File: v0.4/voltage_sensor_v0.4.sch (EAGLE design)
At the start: 56 parts, among them IC1 AP2112K-3.3TRG1, J1 1017505, J2 20020316-H021B01LF, J9 RJ11-6, M1 MOV-14D431KTR, M2 MOV-14D431KTR, M3 MOV-14D431KTR, T1 ZMPT101B, T2 ZMPT101B, T3 ZMPT101B

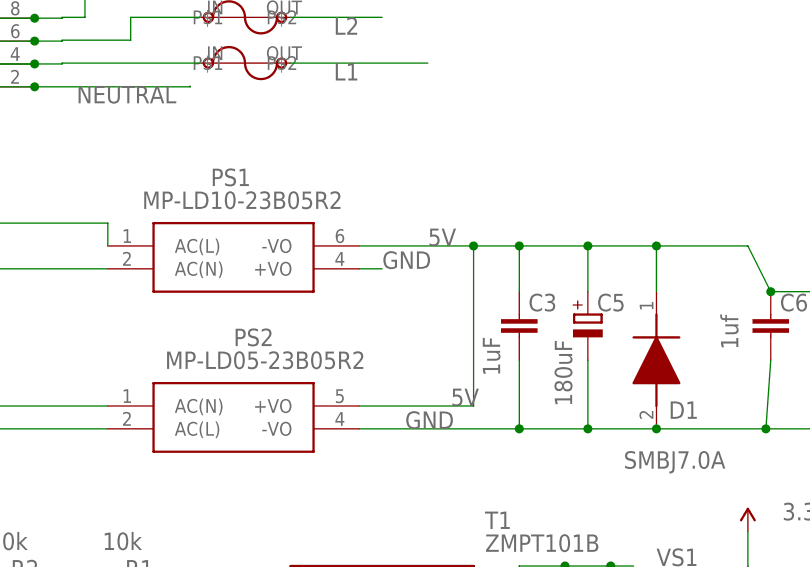
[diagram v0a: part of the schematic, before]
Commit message: fix PSU 10W footprint
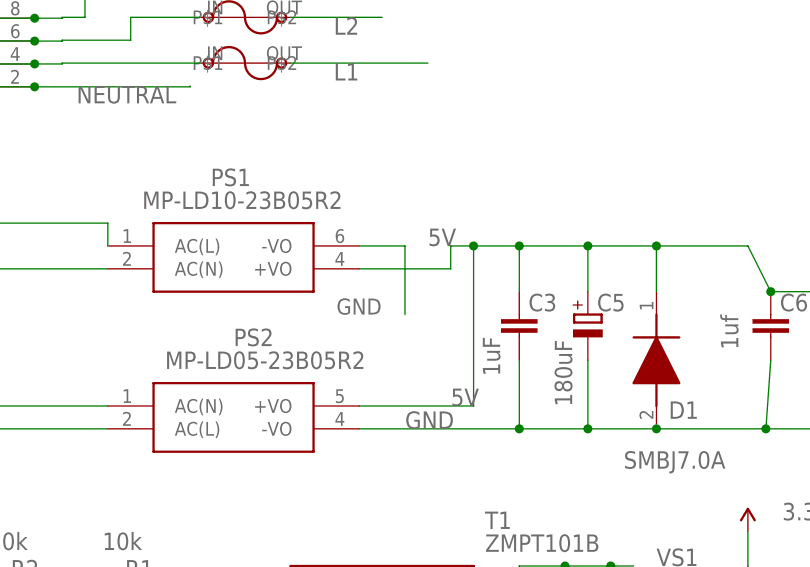
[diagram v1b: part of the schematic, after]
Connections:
- net 5V: now also PS1.+VO; no longer PS1.-VO
- net GND: now also PS1.-VO; no longer PS1.+VO
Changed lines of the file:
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@@
 <grid distance="0.1" unitdist="inch" unit="inch" style="lines" multiple="1" display="no" altdistance="0.01" altunitdist="inch" altunit="inch"/>
 <layers>
-<layer number="1" name="Top" color="4" fill="1" visible="yes" active="no"/>
-<layer number="16" name="Bottom" color="1" fill="1" visible="yes" active="no"/>
-<layer number="17" name="Pads" color="2" fill="1" visible="yes" active="no"/>
-<layer number="18" name="Vias" color="2" fill="1" visible="yes" active="no"/>
-<layer number="19" name="Unrouted" color="6" fill="1" visible="yes" active="no"/>
-<layer number="20" name="Dimension" color="24" fill="1" visible="yes" active="no"/>
-<layer number="21" name="tPlace" color="7" fill="1" visible="yes" active="no"/>
-<layer number="22" name="bPlace" color="7" fill="1" visible="yes" active="no"/>
-<layer number="23" name="tOrigins" color="15" fill="1" visible="yes" active="no"/>
-<layer number="24" name="bOrigins" color="15" fill="1" visible="yes" active="no"/>
-<layer number="25" name="tNames" color="7" fill="1" visible="yes" active="no"/>
-<layer number="26" name="bNames" color="7" fill="1" visible="yes" active="no"/>
-<layer number="27" name="tValues" color="7" fill="1" visible="yes" active="no"/>
-<layer number="28" name="bValues" color="7" fill="1" visible="yes" active="no"/>
+<layer number="1" name="Top" color="4" fill="1" visible="no" active="no"/>
+<layer number="16" name="Bottom" color="1" fill="1" visible="no" active="no"/>
+<layer number="17" name="Pads" color="2" fill="1" visible="no" active="no"/>
+<layer number="18" name="Vias" color="2" fill="1" visible="no" active="no"/>
+<layer number="19" name="Unrouted" color="6" fill="1" visible="no" active="no"/>
+<layer number="20" name="Dimension" color="24" fill="1" visible="no" active="no"/>
+<layer number="21" name="tPlace" color="7" fill="1" visible="no" active="no"/>
+<layer number="22" name="bPlace" color="7" fill="1" visible="no" active="no"/>
+<layer number="23" name="tOrigins" color="15" fill="1" visible="no" active="no"/>
+<layer number="24" name="bOrigins" color="15" fill="1" visible="no" active="no"/>
+<layer number="25" name="tNames" color="7" fill="1" visible="no" active="no"/>
+<layer number="26" name="bNames" color="7" fill="1" visible="no" active="no"/>
+<layer number="27" name="tValues" color="7" fill="1" visible="no" active="no"/>
+<layer number="28" name="bValues" color="7" fill="1" visible="no" active="no"/>
 <layer number="29" name="tStop" color="7" fill="3" visible="no" active="no"/>
 <layer number="30" name="bStop" color="7" fill="6" visible="no" active="no"/>
@@
 <layer number="35" name="tGlue" color="7" fill="4" visible="no" active="no"/>
 <layer number="36" name="bGlue" color="7" fill="5" visible="no" active="no"/>
-<layer number="37" name="tTest" color="7" fill="1" visible="yes" active="no"/>
-<layer number="38" name="bTest" color="7" fill="1" visible="yes" active="no"/>
+<layer number="37" name="tTest" color="7" fill="1" visible="no" active="no"/>
+<layer number="38" name="bTest" color="7" fill="1" visible="no" active="no"/>
 <layer number="39" name="tKeepout" color="4" fill="11" visible="no" active="no"/>
 <layer number="40" name="bKeepout" color="1" fill="11" visible="no" active="no"/>
@@
 <layer number="44" name="Drills" color="7" fill="1" visible="no" active="no"/>
 <layer number="45" name="Holes" color="7" fill="1" visible="no" active="no"/>
-<layer number="46" name="Milling" color="3" fill="1" visible="yes" active="no"/>
-<layer number="47" name="Measures" color="7" fill="1" visible="yes" active="no"/>
-<layer number="48" name="Document" color="7" fill="1" visible="yes" active="no"/>
-<layer number="49" name="Reference" color="7" fill="1" visible="yes" active="no"/>
-<layer number="50" name="dxf" color="7" fill="1" visible="yes" active="no"/>
-<layer number="51" name="tDocu" color="7" fill="1" visible="yes" active="no"/>
-<layer number="52" name="bDocu" color="7" fill="1" visible="yes" active="no"/>
-<layer number="53" name="tGND_GNDA" color="7" fill="9" visible="yes" active="no"/>
-<layer number="54" name="bGND_GNDA" color="1" fill="9" visible="yes" active="no"/>
-<layer number="56" name="wert" color="7" fill="1" visible="yes" active="no"/>
-<layer number="57" name="tCAD" color="7" fill="1" visible="yes" active="no"/>
-<layer number="58" name="bCAD" color="11" fill="1" visible="yes" active="no"/>
-<layer number="59" name="tCarbon" color="7" fill="1" visible="yes" active="no"/>
-<layer number="60" name="bCarbon" color="7" fill="1" visible="yes" active="no"/>
-<layer number="61" name="stand" color="7" fill="1" visible="yes" active="no"/>
+<layer number="46" name="Milling" color="3" fill="1" visible="no" active="no"/>
+<layer number="47" name="Measures" color="7" fill="1" visible="no" active="no"/>
+<layer number="48" name="Document" color="7" fill="1" visible="no" active="no"/>
+<layer number="49" name="Reference" color="7" fill="1" visible="no" active="no"/>
+<layer number="50" name="dxf" color="7" fill="1" visible="no" active="no"/>
+<layer number="51" name="tDocu" color="7" fill="1" visible="no" active="no"/>
+<layer number="52" name="bDocu" color="7" fill="1" visible="no" active="no"/>
+<layer number="53" name="tGND_GNDA" color="7" fill="9" visible="no" active="no"/>
+<layer number="54" name="bGND_GNDA" color="1" fill="9" visible="no" active="no"/>
+<layer number="56" name="wert" color="7" fill="1" visible="no" active="no"/>
+<layer number="57" name="tCAD" color="7" fill="1" visible="no" active="no"/>
+<layer number="58" name="bCAD" color="11" fill="1" visible="no" active="no"/>
+<layer number="59" name="tCarbon" color="7" fill="1" visible="no" active="no"/>
+<layer number="60" name="bCarbon" color="7" fill="1" visible="no" active="no"/>
+<layer number="61" name="stand" color="7" fill="1" visible="no" active="no"/>
 <layer number="88" name="SimResults" color="9" fill="1" visible="yes" active="yes"/>
 <layer number="89" name="SimProbes" color="9" fill="1" visible="yes" active="yes"/>
@@
 </segment>
 <segment>
-<pinref part="PS1" gate="G$1" pin="+VO"/>
-<wire x1="25.4" y1="76.2" x2="27.94" y2="76.2" width="0.1524" layer="91"/>
-<label x="27.94" y="76.2" size="1.9304" layer="95"/>
-</segment>
-<segment>
 <pinref part="PS2" gate="G$1" pin="-VO"/>
 <label x="30.48" y="58.42" size="1.9304" layer="95"/>
@@
 <pinref part="J2" gate="G$1" pin="1"/>
 </segment>
+<segment>
+<pinref part="PS1" gate="G$1" pin="-VO"/>
+<wire x1="25.4" y1="78.74" x2="30.48" y2="78.74" width="0.1524" layer="91"/>
+<wire x1="30.48" y1="78.74" x2="30.48" y2="71.12" width="0.1524" layer="91"/>
+<label x="22.86" y="71.12" size="1.778" layer="95"/>
+</segment>
 </net>
 <net name="N$25" class="0">
@@
 </segment>
 <segment>
-<pinref part="PS1" gate="G$1" pin="-VO"/>
-<wire x1="25.4" y1="78.74" x2="38.1" y2="78.74" width="0.1524" layer="91"/>
 <label x="33.02" y="78.74" size="1.9304" layer="95"/>
 <pinref part="PS2" gate="G$1" pin="+VO"/>
@@
 <wire x1="43.18" y1="73.66" x2="43.18" y2="78.74" width="0.1524" layer="91"/>
 <wire x1="43.18" y1="78.74" x2="38.1" y2="78.74" width="0.1524" layer="91"/>
-<junction x="38.1" y="78.74"/>
 <wire x1="43.18" y1="78.74" x2="50.8" y2="78.74" width="0.1524" layer="91"/>
 <junction x="43.18" y="78.74"/>
@@
 <wire x1="58.42" y1="73.66" x2="58.42" y2="78.74" width="0.1524" layer="91"/>
 <junction x="58.42" y="78.74"/>
-</segment>
-<segment>
+<pinref part="PS1" gate="G$1" pin="+VO"/>
+<wire x1="25.4" y1="76.2" x2="35.56" y2="76.2" width="0.1524" layer="91"/>
+<wire x1="35.56" y1="76.2" x2="35.56" y2="78.74" width="0.1524" layer="91"/>
+<wire x1="35.56" y1="78.74" x2="38.1" y2="78.74" width="0.1524" layer="91"/>
+<junction x="38.1" y="78.74"/>
+</segment>
+<segment>

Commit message: fiducials
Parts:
- added FD1, FD2, FD3: FIDUCIAL1X2, SparkFun-Aesthetics:FIDUCIAL1X2
- added LOGO1: ROHS_LOGO, SparkFun-Aesthetics:ROHS_LOGO
- added LOGO2: OSHW-LOGOS-COPPER, SparkFun-Aesthetics:OSHW-LOGOS-COPPER
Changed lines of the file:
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@@
 <part name="J1" library="1017505" deviceset="1017505" device=""/>
 <part name="J2" library="20020316-H021B01LF" deviceset="20020316-H021B01LF" device=""/>
+<part name="FD1" library="SparkFun-Aesthetics" deviceset="FIDUCIAL" device="1X2"/>
+<part name="FD2" library="SparkFun-Aesthetics" deviceset="FIDUCIAL" device="1X2"/>
+<part name="FD3" library="SparkFun-Aesthetics" deviceset="FIDUCIAL" device="1X2"/>
+<part name="FRAME1" library="SparkFun-Aesthetics" deviceset="FRAME-A4L" device=""/>
+<part name="LOGO1" library="SparkFun-Aesthetics" deviceset="ROHS_LOGO" device=""/>
+<part name="LOGO2" library="SparkFun-Aesthetics" deviceset="OSHW-LOGO" device="S-COPPER"/>
 </parts>
 <sheets>
@@
 <attribute name="VALUE" x="105.41" y="-15.24" size="1.778" layer="96" rot="R180" align="center-left"/>
 </instance>
+<instance part="FD1" gate="G$1" x="43.18" y="109.22" smashed="yes"/>
+<instance part="FD2" gate="G$1" x="43.18" y="104.14" smashed="yes"/>
+<instance part="FD3" gate="G$1" x="43.18" y="99.06" smashed="yes"/>
+<instance part="FRAME1" gate="G$1" x="-81.28" y="-55.88" smashed="yes">
+<attribute name="DRAWING_NAME" x="100.33" y="-44.45" size="2.54" layer="94" font="vector"/>
+<attribute name="LAST_DATE_TIME" x="100.33" y="-49.53" size="2.286" layer="94" font="vector"/>
+<attribute name="SHEET" x="114.3" y="-54.61" size="2.54" layer="94" font="vector"/>
+<attribute name="DESIGNER" x="144.98" y="-49.53" size="2.54" layer="94" font="vector"/>
+</instance>
+<instance part="LOGO1" gate="G$1" x="50.8" y="93.98" smashed="yes"/>
+<instance part="LOGO2" gate="G$1" x="86.36" y="104.14" smashed="yes"/>
 </instances>
 <busses>

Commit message: add filter components
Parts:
- added C4: B32923C3105M000, B32923C3105M000:B32923C3105M000
- added U$1: 47mH, Schaffner-CM-Choke:RN114-0.3-02-47M
- added U$2: RN214-0.3-02-47M, Schaffner-CM-Choke:RN214-0.3-02-47M
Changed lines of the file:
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@@
 <part name="LOGO1" library="SparkFun-Aesthetics" deviceset="ROHS_LOGO" device=""/>
 <part name="LOGO2" library="SparkFun-Aesthetics" deviceset="OSHW-LOGO" device="S-COPPER"/>
+<part name="U$2" library="Schaffner-CM-Choke" deviceset="RN214-0.3-02-47M" device=""/>
+<part name="U$1" library="Schaffner-CM-Choke" deviceset="RN114-0.3-02-47M" device="" value="47mH"/>
+<part name="C4" library="B32923C3105M000" deviceset="B32923C3105M000" device=""/>
 </parts>
 <sheets>
@@
 <attribute name="VALUE" x="105.41" y="-15.24" size="1.778" layer="96" rot="R180" align="center-left"/>
 </instance>
-<instance part="FD1" gate="G$1" x="43.18" y="109.22" smashed="yes"/>
-<instance part="FD2" gate="G$1" x="43.18" y="104.14" smashed="yes"/>
-<instance part="FD3" gate="G$1" x="43.18" y="99.06" smashed="yes"/>
+<instance part="FD1" gate="G$1" x="129.54" y="111.76" smashed="yes"/>
+<instance part="FD2" gate="G$1" x="129.54" y="106.68" smashed="yes"/>
+<instance part="FD3" gate="G$1" x="129.54" y="101.6" smashed="yes"/>
 <instance part="FRAME1" gate="G$1" x="-81.28" y="-55.88" smashed="yes">
 <attribute name="DRAWING_NAME" x="100.33" y="-44.45" size="2.54" layer="94" font="vector"/>
@@
 <attribute name="DESIGNER" x="144.98" y="-49.53" size="2.54" layer="94" font="vector"/>
 </instance>
-<instance part="LOGO1" gate="G$1" x="50.8" y="93.98" smashed="yes"/>
-<instance part="LOGO2" gate="G$1" x="86.36" y="104.14" smashed="yes"/>
+<instance part="LOGO1" gate="G$1" x="137.16" y="96.52" smashed="yes"/>
+<instance part="LOGO2" gate="G$1" x="172.72" y="106.68" smashed="yes"/>
+<instance part="U$2" gate="G$1" x="66.04" y="81.28" smashed="yes"/>
+<instance part="U$1" gate="G$1" x="66.04" y="99.06" smashed="yes"/>
+<instance part="C4" gate="G$1" x="45.72" y="86.36" smashed="yes" rot="R90">
+<attribute name="NAME" x="52.07" y="92.71" size="1.778" layer="95" rot="R180" align="center-left"/>
+<attribute name="VALUE" x="44.45" y="90.17" size="1.778" layer="96" rot="R180" align="center-left"/>
+</instance>
 </instances>
 <busses>
